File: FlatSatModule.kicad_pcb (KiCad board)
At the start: 4 copper layers, 110.2 x 119.4 mm, 8 parts, among them J1 DB26_Male_HighDensity_Mountin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, J2 Micro_SD_Card_Det, J3 HEADER_13x2

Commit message: Redo routing
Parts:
- moved J3 31.1 mm to (95.2, 99.1), turned to 180 degrees
- moved D2 20.3 mm to (67.1, 127.0), turned to 180 degrees
- moved R2 18.7 mm to (72.8, 127.0)
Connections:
- J2 pad 11: Net-(J2-Pad11) -> GND
- J2 pad 3: /SD_CMD -> /PD2
- J2 pad 5: /SD_CLK -> /PC12
- J3 pad 1: Net-(J3-Pad1) -> VCC
- J3 pad 12: Net-(J3-Pad12) -> /PA10
- J3 pad 14: Net-(J3-Pad14) -> /PA9
- J3 pad 16: Net-(J3-Pad16) -> /PE4
- J3 pad 18: Net-(J3-Pad18) -> /PE2
- J3 pad 2: Net-(J3-Pad2) -> GND
- J3 pad 20: Net-(J3-Pad20) -> /PE5
- J3 pad 22: Net-(J3-Pad22) -> /PE6
- J3 pad 24: Net-(J3-Pad24) -> /I2C2_SDA
- J3 pad 26: Net-(J3-Pad26) -> /I2C2_SCL
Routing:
- net /SD_DETA: track 0.00 -> 159.5 mm, vias 0 -> 2
- net /I2C2_SCL: track 0.00 -> 115.7 mm
- net /I2C2_SDA: track 0.00 -> 114.7 mm
- net /PA2: track 0.00 -> 97.9 mm
- net /PA4: track 0.00 -> 93.9 mm
- net /PA5: track 0.00 -> 91.1 mm
- net /PA7: track 0.00 -> 89.5 mm
- net /PA3: track 0.00 -> 88.8 mm
- net /PA9: track 0.00 -> 68.0 mm, vias 0 -> 1
- net /PA10: track 0.00 -> 64.9 mm
- net /CAN1_RX: track 0.00 -> 64.4 mm
- net /CAN1_TX: track 0.00 -> 60.8 mm
- net VCC: track 0.00 -> 60.5 mm
- net /I2C1_SDA: track 0.00 -> 49.8 mm
- net /I2C1_SCL: track 0.00 -> 47.9 mm
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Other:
- rule trace_min: 0.2 -> 0.00015

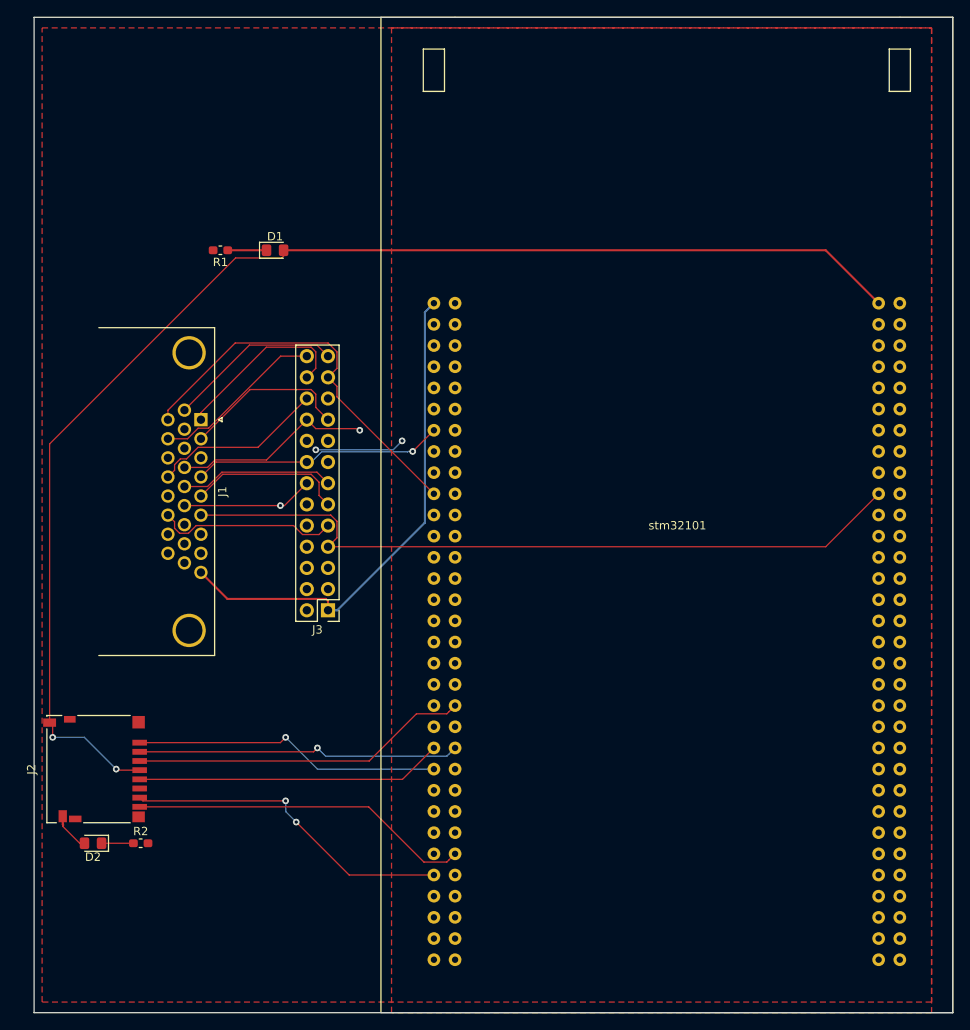
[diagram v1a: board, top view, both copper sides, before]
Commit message: Fix track size
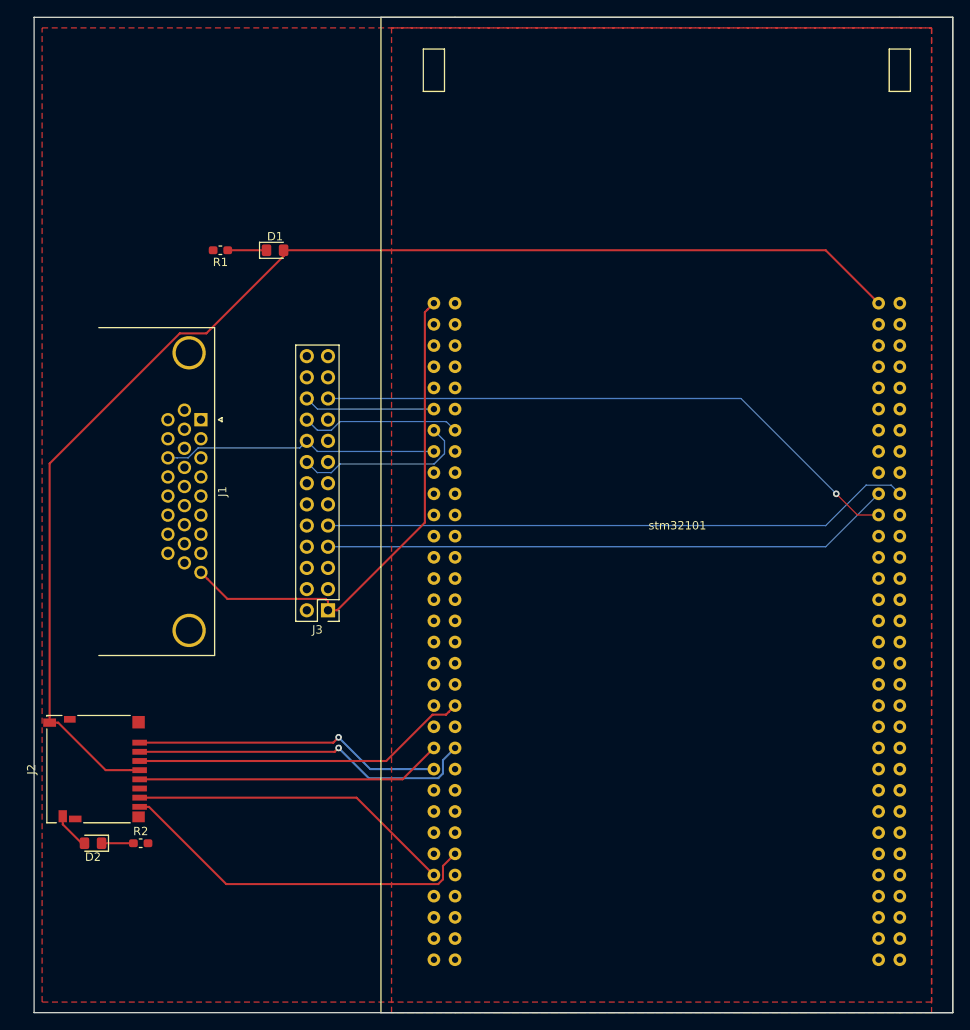
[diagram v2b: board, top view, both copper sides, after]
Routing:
- net /I2C2_SDA: track 114.7 -> 105.6 mm
- net /PA2: track 97.9 -> 91.5 mm
- net /I2C1_SCL: track 47.9 -> 42.1 mm
- net /PE4: track 30.3 -> 34.8 mm, vias 1 -> 0
- net /PA7: track 89.5 -> 93.9 mm
- net /PE2: track 37.3 -> 33.3 mm, vias 2 -> 0
- net /PA3: track 88.8 -> 85.5 mm
- net /PC11: track 38.8 -> 42.0 mm
- net /PC9: track 41.0 -> 44.1 mm
- net /CAN1_TX: track 60.8 -> 57.8 mm
- net /SD_DETA: track 159.5 -> 157.3 mm, vias 2 -> 0
- net /PB4: track 41.9 -> 40.4 mm
- net /I2C2_SCL: track 115.7 -> 116.9 mm
- net /SD_DET: track 5.74 -> 4.52 mm
- net /PA9: track 68.0 -> 66.9 mm, vias 1 -> 0
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
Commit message: Added silkscreen text
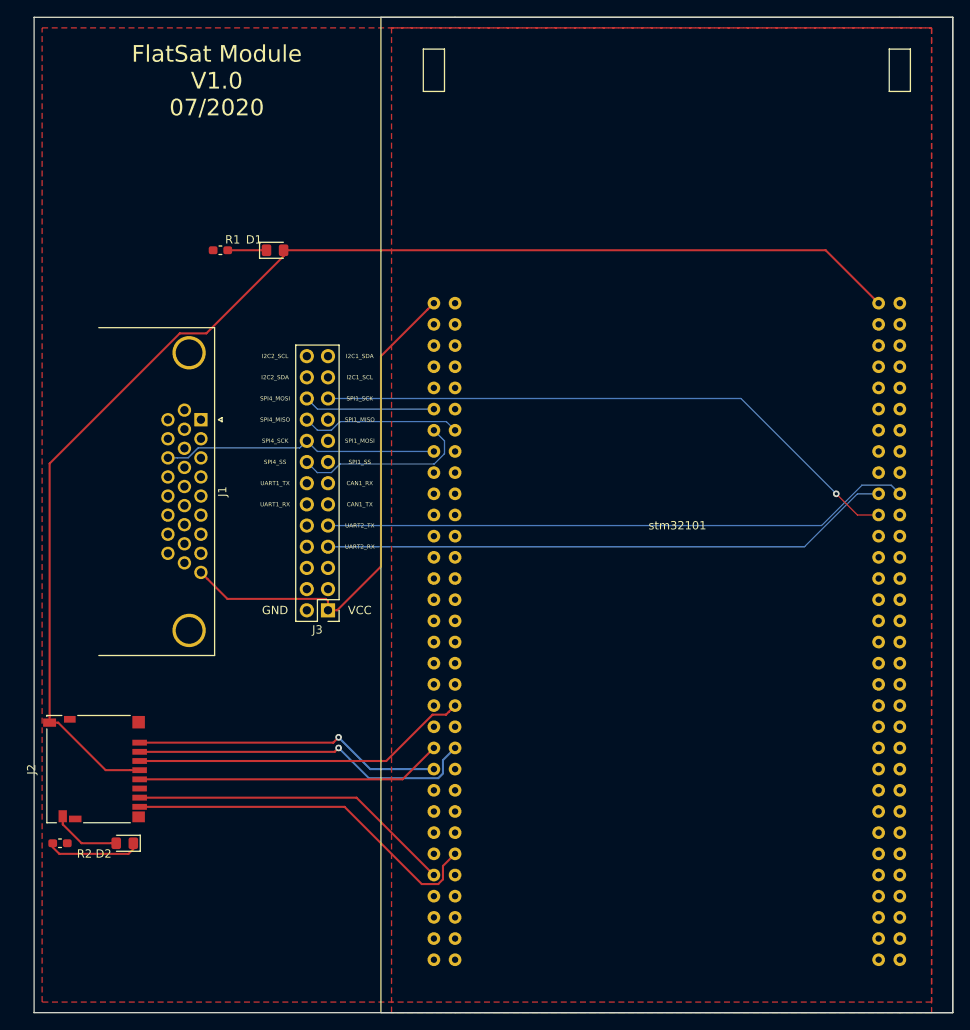
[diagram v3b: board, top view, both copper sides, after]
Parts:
- moved R2 9.68 mm to (63.1, 127.0)
- moved D2 3.81 mm to (70.9, 127.0)
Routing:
- net Net-(D2-Pad1): track 3.82 -> 11.4 mm
- net /SD_DET: track 4.52 -> 8.33 mm
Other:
- board text added: "CAN1_RX"
- board text added: "CAN1_TX"
- board text added: "FlatSat Module V1.0 07/2020"
- board text added: "GND"
- board text added: "I2C1_SCL"
- board text added: "I2C1_SDA"
- board text added: "I2C2_SCL"
- board text added: "I2C2_SDA"
- board text added: "SPI1_MISO"
- board text added: "SPI1_MOSI"
- board text added: "SPI1_SCK"
- board text added: "SPI1_SS"
- board text added: "SPI4_MISO"
- board text added: "SPI4_MOSI"
- board text added: "SPI4_SCK"
- board text added: "SPI4_SS"
- board text added: "UART1_RX"
- board text added: "UART1_TX"
- board text added: "UART2_RX"
- board text added: "UART2_TX"
- board text added: "VCC"

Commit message: improve schematic and replace footprints
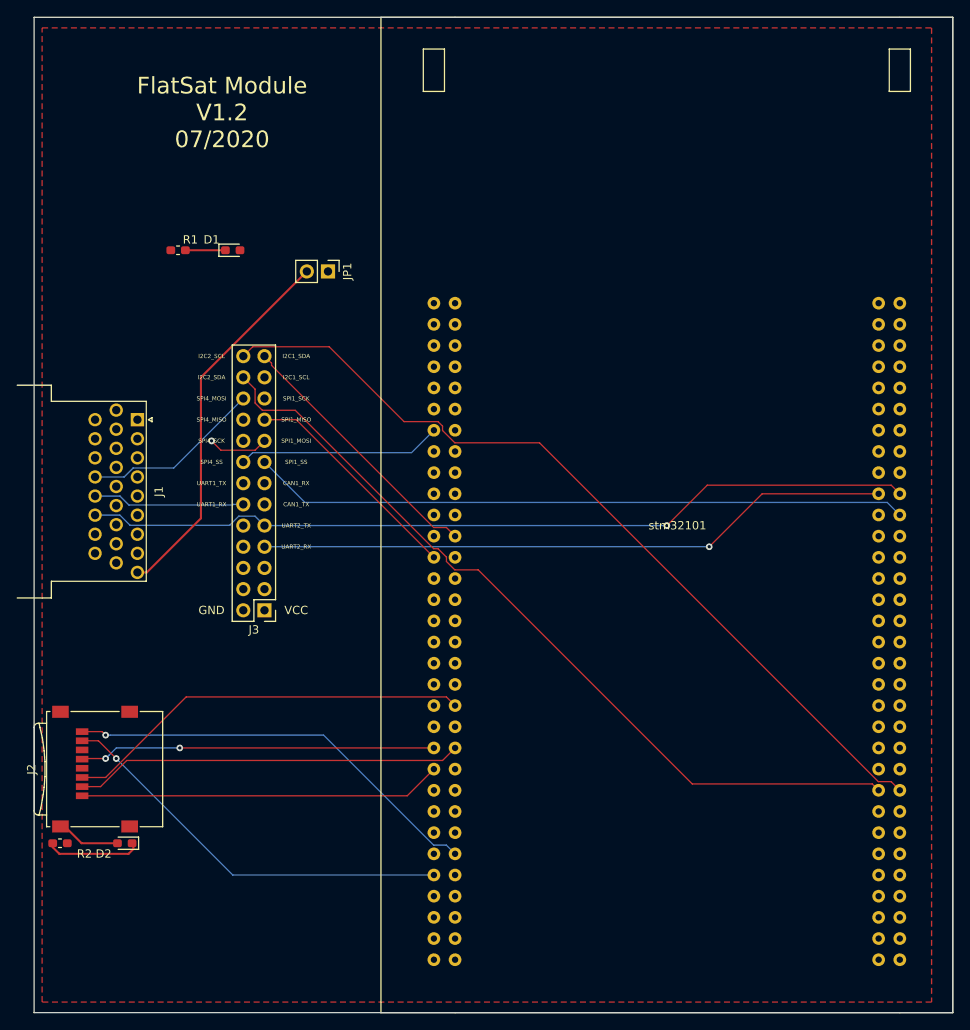
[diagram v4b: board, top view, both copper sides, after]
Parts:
- added JP1: Jumper_2_Bridged, Connector_PinHeader_2.54mm:PinHeader_1x02_P2.54mm_Vertical, F.Cu at (95.2, 58.4)
- D1, D2: footprint LED_SMD:LED_0805_2012Metric_Pad1.15x1.40mm_HandSolder -> LED_SMD:LED_0603_1608Metric_Pad1.05x0.95mm_HandSolder
- J1: footprint Connector_Dsub:DSUB-26-HD_Male_Horizontal_P2.29x1.98mm_EdgePinOffset8.35mm_Housed_MountingHolesOffset10.89mm -> Connector_Dsub:DSUB-26-HD_Male_Horizontal_P2.29x2.54mm_EdgePinOffset9.40mm
- J2: footprint Connector_Card:microSD_HC_Hirose_DM3D-SF -> Connector_Card:microSD_HC_Wuerth_693072010801
- moved J1 7.62 mm to (72.4, 76.2)
- moved J3 7.62 mm to (87.6, 99.1)
- moved D1 5.08 mm to (83.8, 55.9)
- moved R1 5.08 mm to (77.3, 55.9)
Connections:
- net /PA10 renamed /UART1_RX
- net /PA2 renamed /UART2_TX
- net /PA3 renamed /UART2_RX
- net /PA4 renamed /SPI1_SS
- net /PA5 renamed /SPI1_SCK
- net /PA7 renamed /SPI1_MOSI
- net /PA9 renamed /UART1_TX
- net /PB4 renamed /SPI1_MISO
- net /PC10 renamed /SD_D2
- net /PC11 renamed /SD_D3
- net /PC12 renamed /SD_CLK
- net /PC8 renamed /SD_D0
- net /PC9 renamed /SD_D1
- net /PD2 renamed /SD_CMD
- net /PE2 renamed /SPI4_SCK
- net /PE4 renamed /SPI4_SS
- net /PE5 renamed /SPI4_MISO
- net /PE6 renamed /SPI4_MOSI
- D1 pad 2: /SD_DETA -> VCC
- J1 pad 9: VCC -> Net-(J1-Pad9)
- J2 pad 4: /SD_DETA -> VCC
- J3 pad 1: VCC -> /5V
- J3 pad 4: Net-(J3-Pad4) -> VCC
- stm32101 pad 1: VCC -> /5V
- stm32101 pad 128: Net-(stm32101-Pad128) -> GND
- stm32101 pad 2: Net-(stm32101-Pad2) -> /5V
- stm32101 pad 64: Net-(stm32101-Pad64) -> GND
- stm32101 pad 65: /SD_DETA -> VCC
- stm32101 pad 66: Net-(stm32101-Pad66) -> VCC
- stm32101 pad 75: Net-(stm32101-Pad75) -> GND
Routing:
- net /SD_DETA: track 157.3 -> 0.00 mm
- net VCC: track 60.5 -> 0.00 mm
- net Net-(J1-Pad9): track 0.00 -> 45.2 mm
- net /SPI4_SCK: track 33.3 -> 18.6 mm
- net /SD_D0: track 39.1 -> 48.9 mm, vias 0 -> 1
- net /UART2_TX: track 91.5 -> 100.4 mm, vias 0 -> 1
- net /SD_CMD: track 40.6 -> 49.2 mm
- net /SPI4_MOSI: track 36.8 -> 45.1 mm
- net /I2C2_SDA: track 105.6 -> 113.4 mm
- net /UART2_RX: track 85.5 -> 93.1 mm, vias 0 -> 1
- net /SPI1_SCK: track 91.5 -> 99.1 mm, vias 1 -> 0
- net /SPI4_MISO: track 36.2 -> 43.7 mm
- net /I2C1_SCL: track 42.1 -> 49.6 mm
- net /SD_D1: track 44.1 -> 50.8 mm, vias 0 -> 1
- net /I2C2_SCL: track 116.9 -> 123.5 mm
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- added copper zone on In2.Cu, net /5V
- added copper zone on In1.Cu, net VCC
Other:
- board text added: "FlatSat Module V1.2 07/2020"
- board text removed: "FlatSat Module V1.0 07/2020"

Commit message: Add mounting holes, replace microSD footprint and move components
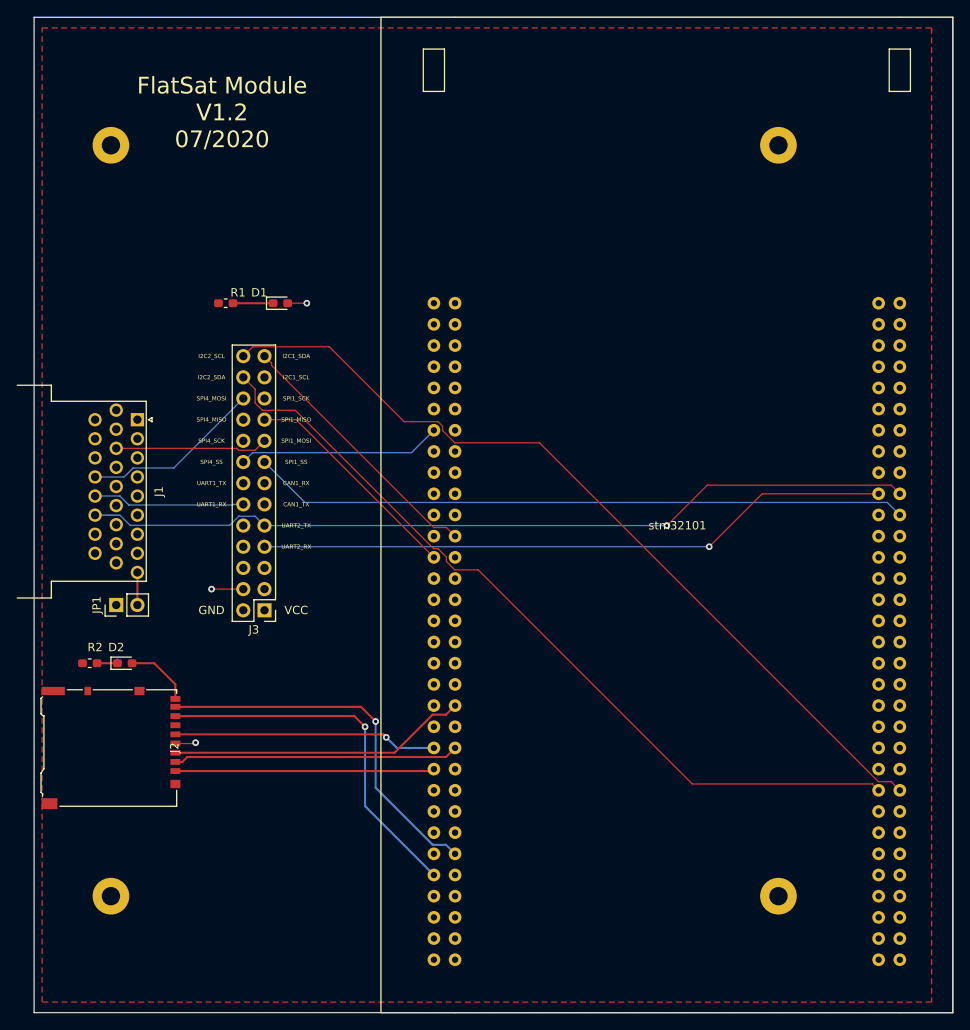
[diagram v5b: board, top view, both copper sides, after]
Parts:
- added REF**: MountingHole_2.2mm_M2_Pad, MountingHole:MountingHole_2.2mm_M2_Pad, F.Cu at (149.3, 133.3)
- added REF**: MountingHole_2.2mm_M2_Pad, MountingHole:MountingHole_2.2mm_M2_Pad, F.Cu at (69.2, 133.3)
- added REF**: MountingHole_2.2mm_M2_Pad, MountingHole:MountingHole_2.2mm_M2_Pad, F.Cu at (149.3, 43.3)
- added REF**: MountingHole_2.2mm_M2_Pad, MountingHole:MountingHole_2.2mm_M2_Pad, F.Cu at (69.2, 43.3)
- J2: footprint Connector_Card:microSD_HC_Wuerth_693072010801 -> Connector_Card:microSD_HC_Hirose_DM3AT-SF-PEJM5
- moved JP1 47.4 mm to (69.8, 98.4), turned to 90 degrees
- moved R2 21.9 mm to (66.7, 105.4), turned to 180 degrees
- moved D2 21.6 mm to (70.9, 105.4), turned to 0 degrees
- moved D1 8.54 mm to (89.5, 62.2)
- moved R1 8.54 mm to (83.0, 62.2)
- moved J2 3.18 mm to (69.2, 115.6), turned to 270 degrees
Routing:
- net Net-(J1-Pad9): track 45.2 -> 3.91 mm
- net /SPI4_SCK: track 18.6 -> 42.0 mm
- net /SD_CMD: track 49.2 -> 35.9 mm
- net /SD_D2: track 43.5 -> 31.1 mm
- net /SD_D3: track 46.7 -> 34.2 mm
- net /SD_CLK: track 42.7 -> 31.7 mm, vias 2 -> 1
- net VCC: track 0.00 -> 8.59 mm, vias 0 -> 3
- net Net-(D2-Pad1): track 11.4 -> 2.92 mm
- net /SD_D1: track 50.8 -> 45.5 mm
- net /SD_D0: track 48.9 -> 44.5 mm
- net /SPI1_MOSI: track 97.5 -> 96.7 mm, vias 1 -> 0
- net /SD_DET: track 7.35 -> 7.99 mm
